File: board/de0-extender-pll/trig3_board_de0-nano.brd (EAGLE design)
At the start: 50.5 x 62 mm, 123 parts, among them J12 4p-2.54, J13 BU-SMB-V, J141 2p-2.54, J15 2p-2.54, J16 2p-2.54, J17 2p-2.54, J18 2p-2.54, J22 2p-2.54, J23 2p-2.54, J24 2p-2.54, J25 2p-2.54, J3 4p-2.54, J32 2p-2.54, J33 2p-2.54, J34 2p-2.54, J35 2p-2.54, J36 2p-2.54, J37 2p-2.54, J38 2p-2.54, J39 2p-2.54, J4 2p-2.54, J40 2p-2.54, J41 2p-2.54, J42 2p-2.54, J43 2p-2.54, J5 2p-2.54, J6 2p-2.54, J7 4p-2.54, K15_R10P BU-SMB-V, K16_R10N BU-SMB-V, M16CLK_3N BU-SMB-V, P11 BU-SMB-V, P15 BU-SMB-V, P16_R15N BU-SMB-V, P9 BU-SMB-V, T13_B20N BU-SMB-V, T14_B23P BU-SMB-V, T15_B23N BU-SMB-V, T9CLK_7N BU-SMB-V

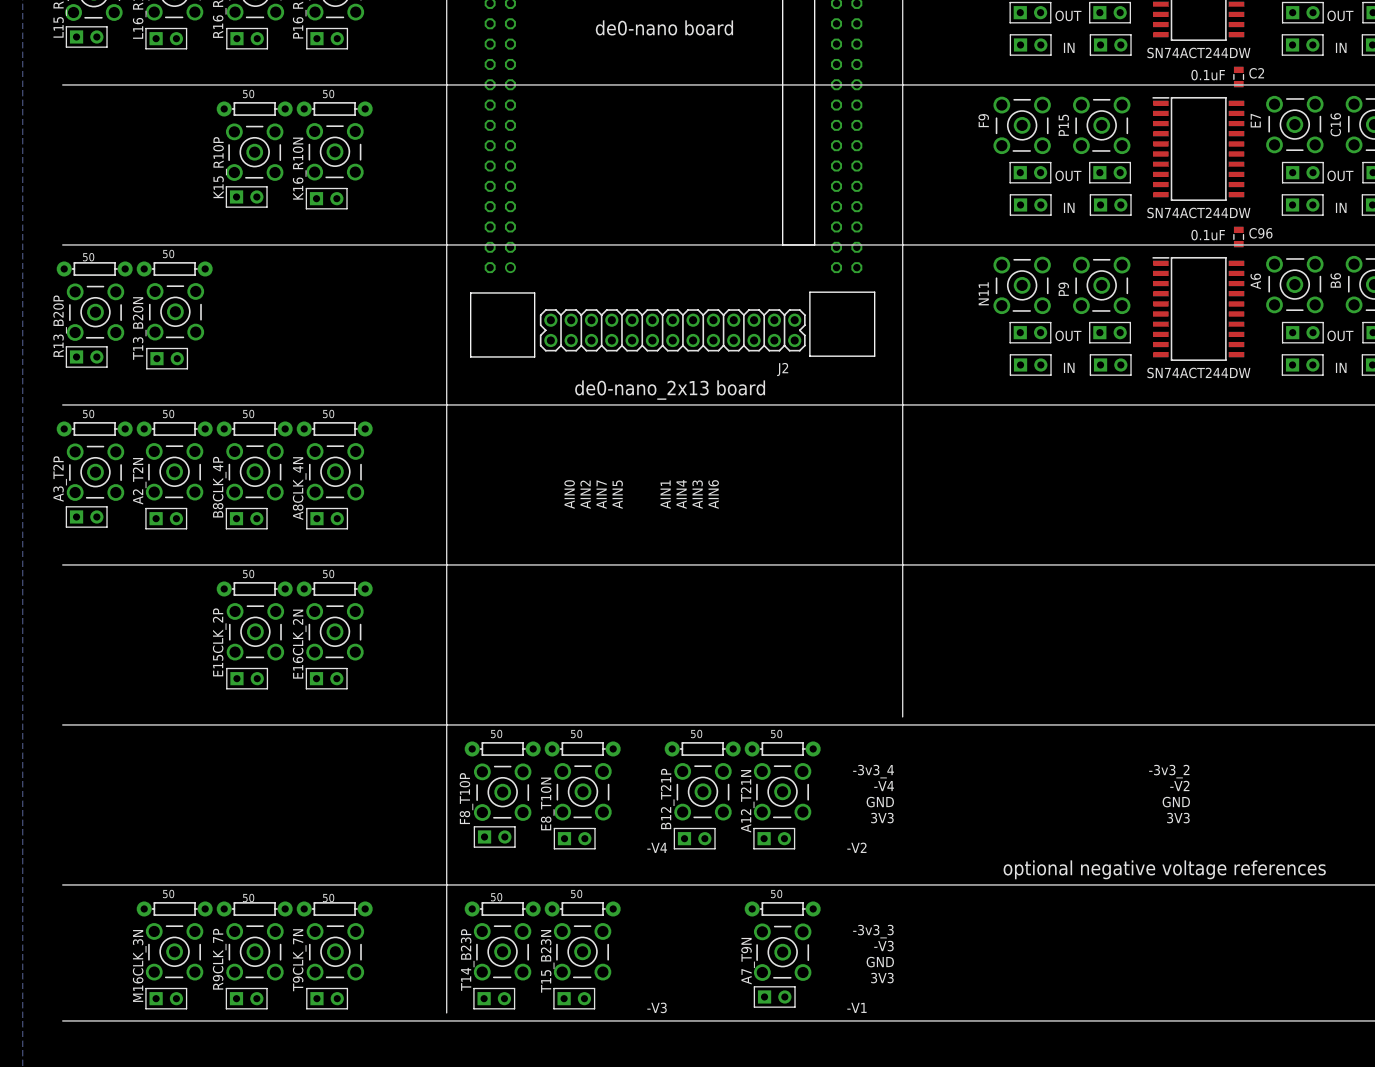
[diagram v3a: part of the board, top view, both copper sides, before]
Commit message: going to delete more ins/outs
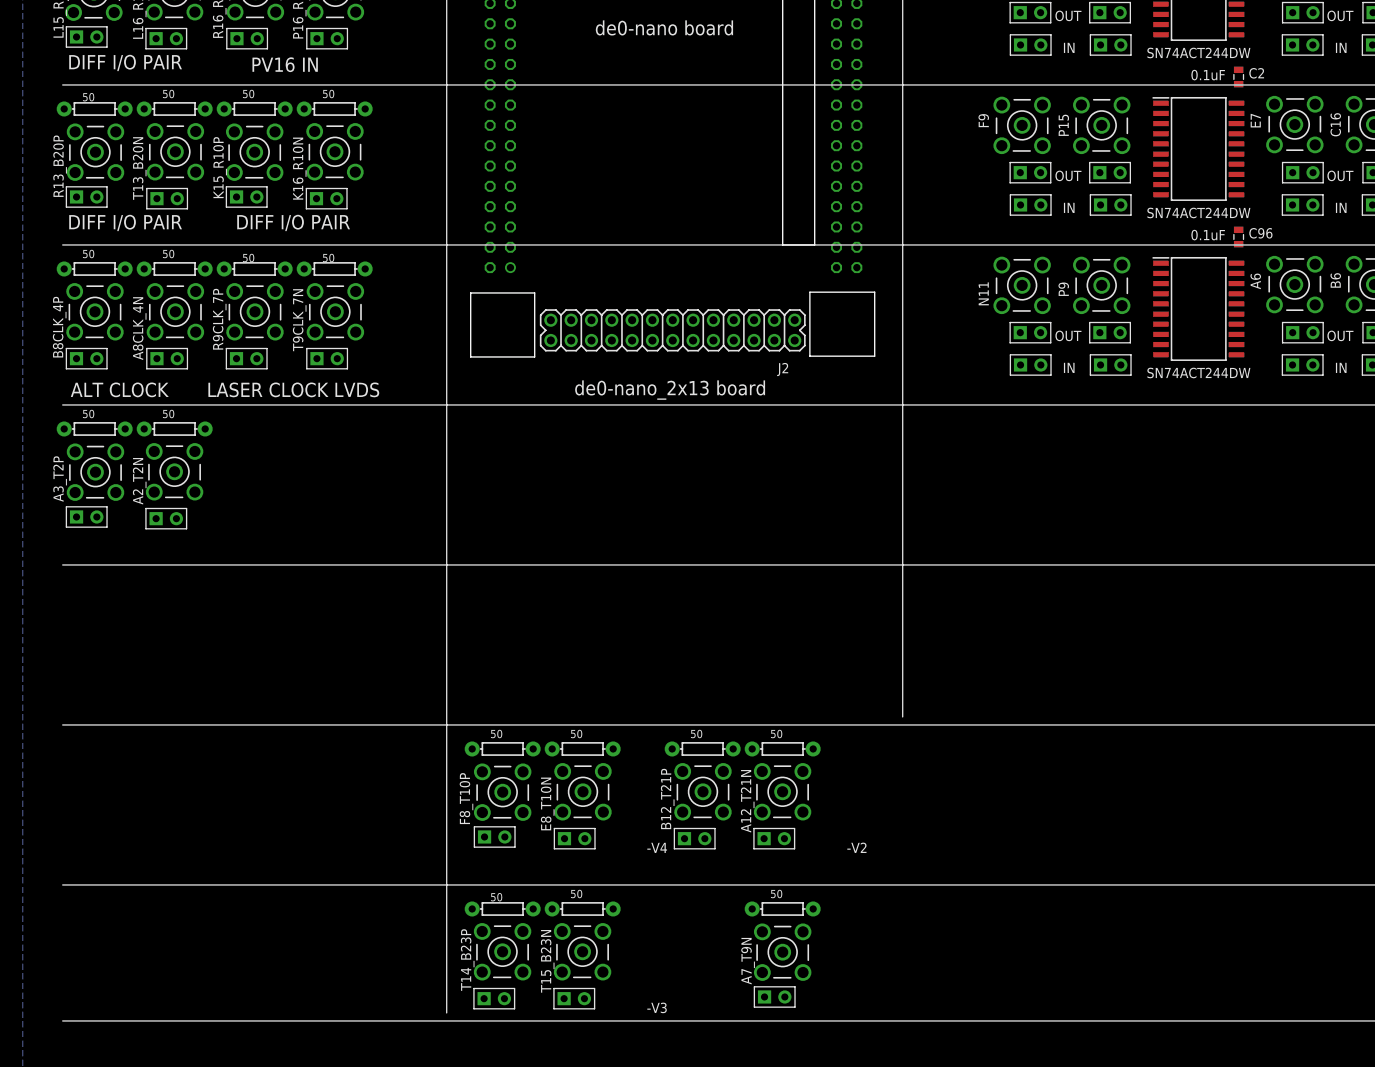
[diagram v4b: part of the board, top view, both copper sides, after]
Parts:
- removed E15CLK_2P, E16CLK_2N, M16CLK_3N: BU-SMB-V, con-coax:BU-SMB-V
- removed J141, J15, J16: 2p-2.54, Seeed-Connector:H2-2.54
- removed R15, R18, R19: 50, SparkFun-Passives:AXIAL-0.3
- moved J5 80.0 mm to (-24.0, 44.8)
- moved J6 80.0 mm to (-13.9, 44.8)
- moved R5 80.0 mm to (-23.0, 56.0)
- moved R6 80.0 mm to (-13.0, 56.0)
- moved R9CLK_7P 80.0 mm to (-23.0, 50.6)
- moved T9CLK_7N 80.0 mm to (-12.9, 50.6)
- moved A8CLK_4N 28.3 mm to (-32.9, 50.6)
- moved B8CLK_4P 28.3 mm to (-43.0, 50.6)
- moved J24 28.3 mm to (-33.9, 44.8)
- moved R22 28.3 mm to (-43.0, 56.0)
- moved R23 28.3 mm to (-33.0, 56.0)
- moved J23 28.3 mm to (-44.0, 44.8)
- moved J38 20.0 mm to (-33.9, 64.8)
- moved T13_B20N 20.0 mm to (-32.9, 70.7)
- moved J17 20.0 mm to (-44.0, 65.0)
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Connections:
- removed net GPIO_2_IN0_E15CLK: E15CLK_2P.1, J16.2, R19.P$2
- removed net GPIO_2_IN1_E16CLK: E16CLK_2N.1, J15.2, R18.P$2
- removed net GPIO_2_IN2_M16CLK: J141.2, M16CLK_3N.1, R15.P$2
- net GND: no longer E15CLK_2P.2, E15CLK_2P.3, E15CLK_2P.4, E15CLK_2P.5, E16CLK_2N.2, E16CLK_2N.3, E16CLK_2N.4, E16CLK_2N.5, J141.1, J15.1, J16.1, M16CLK_3N.2, M16CLK_3N.3, M16CLK_3N.4, M16CLK_3N.5, R15.P$1, R18.P$1, R19.P$1
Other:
- board text added: "ALT CLOCK"
- board text added: "DIFF I/O PAIR"
- board text added: "LASER CLOCK LVDS"
- board text added: "PV16 IN"
- board text removed: "-3v3_2"
- board text removed: "-3v3_3"
- board text removed: "-3v3_4"
- board text removed: "-V1"
- board text removed: "AIN0"
- board text removed: "AIN1"
- board text removed: "AIN2"
- board text removed: "AIN3"
- board text removed: "AIN4"
- board text removed: "AIN5"
- board text removed: "AIN6"
- board text removed: "AIN7"
- board text removed: "optional negative voltage references"
